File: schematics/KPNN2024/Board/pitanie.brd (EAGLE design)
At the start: 100 x 80 mm, 32 parts

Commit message: я смотрел рика и морти вместо работать
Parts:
- added R8: 1k, rcl:R0603
- added TMC: DRIVER_TMC2209, UNKNOWN-2024:DRIVER_TMC2209
- moved R7 138.1 mm to (68.6, 17.8)
- moved U$8 131.2 mm to (78.2, 21.0), turned to 225 degrees
- moved LSM 130.6 mm to (65.9, 48.3), turned to 90 degrees
- moved C8 129.4 mm to (64.8, 20.5)
- moved C10 127.2 mm to (69.9, 21.1)
- moved U$5 126.0 mm to (77.4, 26.4), turned to 270 degrees
- moved C4 120.6 mm to (72.6, 25.8), turned to 180 degrees
- moved LIS 118.3 mm to (39.9, 48.3), turned to 90 degrees
- moved C5 117.4 mm to (67.3, 31.5)
- moved C6 117.4 mm to (63.5, 31.5)
- moved C7 117.4 mm to (59.7, 31.5)
- moved U$2 115.8 mm to (72.9, 29.9), turned to 90 degrees
- moved C11 108.6 mm to (76.8, 30.7)
- moved U$1 106.2 mm to (54.9, 57.0), flipped to the bottom, turned to 180 degrees
- moved C12 103.3 mm to (42.9, 31.1)
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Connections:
- new net 5V: TMC.P$16
- new net A2: R8.2
- new net A3: R8.1, TMC.P$5
- net GND: now also TMC.P$15, TMC.P$8
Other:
- board size 100 x 80 mm -> 85.1 x 84.3 mm

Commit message: ааа платы платы полигоны разводка платы ааааа
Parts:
- C2, C6, C7: device rcl:C0603 -> rcl:C1206
- moved C4 75.7 mm to (47.3, 97.2)
- moved R3 74.0 mm to (44.1, 98.8)
- moved R2 73.8 mm to (40.8, 98.8)
- moved C5 73.2 mm to (44.1, 100.9), turned to 180 degrees
- moved U$2 70.9 mm to (43.1, 94.3), turned to 0 degrees
- moved U$3 70.0 mm to (52.4, 96.2), turned to 90 degrees
- moved R1 67.4 mm to (39.8, 87.6), turned to 270 degrees
- moved C7 58.7 mm to (49.5, 89.3)
- moved C6 57.2 mm to (49.5, 87.0)
- moved C2 48.6 mm to (43.8, 89.4), turned to 180 degrees
- moved C3 47.3 mm to (43.4, 86.9), turned to 180 degrees
- moved C1 46.3 mm to (39.9, 93.8)
- moved U$1 33.8 mm to (35.9, 85.0), flipped to the top, turned to 0 degrees
- moved R5 8.06 mm to (32.2, 36.2)
- moved C9 1.41 mm to (59.0, 23.0)
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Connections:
- removed net N$6: C5.1, C6.2, C7.2, R3.2, U$3.P$1
- net 3V3: now also C5.1, C6.2, C7.2, R3.2, U$3.P$1
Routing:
- net 3V3: track 0.00 -> 44.6 mm
- net GND-OUT: track 0.00 -> 42.7 mm, vias 0 -> 16
- net N$2: track 0.00 -> 14.6 mm, vias 0 -> 2
- net BUS+: track 0.00 -> 14.5 mm
- net N$5: track 0.00 -> 7.26 mm
- net N$1: track 0.00 -> 3.68 mm
- added copper zone on layer 1, net 3V3
- added copper zone on layer 1, net BUS+
- added copper zone on layer 1, net GND-OUT
- added copper zone on layer 1, net N$3
- added copper zone on layer 1, net N$4
- added copper zone on layer 1, net N$5

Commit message: авыпльдыф
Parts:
- C13, C14, C9: device rcl:C0603 -> rcl:C1206
- moved U$5 76.4 mm to (43.0, 94.7), turned to 0 degrees
- moved C8 76.3 mm to (40.0, 94.0), turned to 90 degrees
- moved C11 72.8 mm to (46.4, 96.8), turned to 180 degrees
- moved U$6 70.7 mm to (52.4, 97.2), turned to 90 degrees
- moved C10 70.6 mm to (44.1, 86.8), turned to 180 degrees
- moved C12 70.2 mm to (44.1, 101.3), turned to 180 degrees
- moved C9 68.5 mm to (44.4, 89.9), turned to 180 degrees
- moved R5 63.5 mm to (40.6, 99.2), turned to 180 degrees
- moved C13 63.5 mm to (50.0, 87.4), turned to 0 degrees
- moved C14 63.0 mm to (50.0, 89.9), turned to 0 degrees
- moved R6 62.9 mm to (44.2, 99.2), turned to 0 degrees
- moved C2 45.2 mm to (62.8, 48.4)
- moved C3 45.2 mm to (62.4, 45.9)
- moved C5 45.2 mm to (63.1, 59.9)
- moved U$1 45.2 mm to (54.9, 44.0)
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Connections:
- removed net N$12: C12.1, C13.2, C14.2, R6.2, U$6.P$1
- net 3V3: now also C12.1, C13.2, C14.2, R6.2, U$6.P$1
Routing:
- net 3V3: track 44.6 -> 88.4 mm
- net GND-OUT: track 42.7 -> 85.4 mm, vias 16 -> 32
- net BUS+: track 14.5 -> 29.9 mm
- net N$8: track 0.00 -> 14.2 mm, vias 0 -> 2
- net N$11: track 0.00 -> 7.51 mm
- net N$7: track 0.00 -> 3.93 mm
- added copper zone on layer 1, net N$10
- added copper zone on layer 1, net N$11
- added copper zone on layer 1, net N$9

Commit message: amogus
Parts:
- removed R8: 1k, rcl:R0603
- added U$10: PBS_SMD_X13, UNKNOWN-2024:PBD_SMD_X13
- added U$11: LIS3MDL, UNKNOWN-2024:LIS3MDL
- added U$9: PBS_SMD_X9, UNKNOWN-2024:PBS_SMD_X9
- moved U$1 55.7 mm to (36.7, 96.6), turned to 270 degrees
- moved R1 50.1 mm to (39.3, 92.7), turned to 180 degrees
- moved C3 49.3 mm to (38.6, 89.1), turned to 90 degrees
- moved C6 47.5 mm to (38.7, 83.0), turned to 270 degrees
- moved C2 45.8 mm to (41.1, 88.7), turned to 90 degrees
- moved C7 44.3 mm to (41.0, 83.0), turned to 270 degrees
- moved C1 42.0 mm to (45.5, 92.6), turned to 0 degrees
- moved U$2 39.5 mm to (46.0, 89.4), turned to 270 degrees
- moved U$4 38.1 mm to (72.3, 74.8), turned to 90 degrees
- moved R2 35.2 mm to (50.5, 91.7), turned to 90 degrees
- moved U$3 34.2 mm to (47.9, 80.1), turned to 0 degrees
- moved C4 33.8 mm to (48.9, 85.2), turned to 90 degrees
- moved R3 33.1 mm to (50.5, 88.4), turned to 270 degrees
- moved R4 31.0 mm to (69.5, 79.1), turned to 0 degrees
- moved C5 30.4 mm to (52.6, 88.4), turned to 90 degrees
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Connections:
- net A0 renamed FOTO
- net B10 renamed OE_SR
- removed net A2: R8.2
- removed net A3: R8.1, TMC.P$5
- removed net A5: LIS.P$4, LSM.P$4
- removed net A7: LIS.P$3, LSM.P$3, U$7.14
- removed net B2: U$7.11
- removed net B4: LIS.P$1, LSM.P$1
- new net DIR_DRIVER: TMC.P$1
- new net LATCH_SR: U$7.12
- new net MISO_SR: LSM.P$1, U$11.SDO
- new net MOSI_SR: LSM.P$3, U$11.SDA, U$7.14
- new net SCK_SR: LSM.P$4, U$11.SCL, U$7.11
- new net STEP_DRIVER: TMC.P$2
- net 3V3: now also U$11.UCC, U$7.16; no longer LIS.P$6
- net GND: now also U$11.GND, U$7.8; no longer LIS.P$5
- net Q1: now also U$11.CS; no longer LIS.P$2
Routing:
- net GND-OUT: track 85.4 -> 147.1 mm
- net N$3: track 0.00 -> 3.01 mm
- net BUS+: track 29.9 -> 32.7 mm
- net N$9: track 0.00 -> 1.82 mm
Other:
- board size 85.1 x 84.3 mm -> 68.9 x 68.9 mm

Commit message: отртамгор
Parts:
- removed LIS: LIS3MDL-GY, CanCubeSat:LIS3MDL-GY
- moved U$11 53.7 mm to (59.0, 50.0), turned to 90 degrees
- moved U$1 53.3 mm to (47.3, 44.4), turned to 90 degrees
- moved R2 45.7 mm to (33.5, 49.3), turned to 270 degrees
- moved C1 44.8 mm to (38.5, 48.4), turned to 180 degrees
- moved R1 44.7 mm to (44.7, 48.3), turned to 0 degrees
- moved C5 41.6 mm to (31.4, 52.6), turned to 270 degrees
- moved R3 39.6 mm to (33.5, 52.6), turned to 90 degrees
- moved U$2 38.6 mm to (38.0, 51.6), turned to 90 degrees
- moved C3 37.8 mm to (45.4, 51.9), turned to 270 degrees
- moved C2 36.4 mm to (42.9, 52.3), turned to 270 degrees
- moved C4 32.5 mm to (35.1, 55.8), turned to 270 degrees
- moved U$6 27.2 mm to (54.5, 65.0), turned to 270 degrees
- moved C6 25.9 mm to (45.3, 58.0), turned to 90 degrees
- moved C7 25.2 mm to (43.0, 58.0), turned to 90 degrees
- moved LSM 25.1 mm to (60.9, 30.7), turned to 270 degrees
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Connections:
- new net CE_RADIO: U$9.1
- new net CS_RADIO: U$9.2
- new net IRQ_RADIO: U$9.3
- new net MISO_RADIO: U$9.5
- new net MOSI_RADIO: U$9.4
- new net RX1_BLF: U$10.4
- new net RX2_GPS: U$9.8
- new net SCK_RADIO: U$9.6
- new net SW_AMP: U$9.9
- new net TX1_BLF: U$10.3
- new net TX2_GPS: U$9.7
- net 3V3: now also U$10.13
- net 5V: now also U$10.11
- net DIR_DRIVER: now also U$10.1
- net FOTO: now also U$10.10
- net GND: now also U$10.12
- net LATCH_SR: now also U$10.5
- net MISO_SR: now also U$10.8
- net MOSI_SR: now also U$10.9
- net OE_SR: now also U$10.6
- net SCK_SR: now also U$10.7
- net STEP_DRIVER: now also U$10.2
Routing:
- net GND: track 0.00 -> 124.7 mm, vias 0 -> 2
- net 3V3: track 88.3 -> 172.1 mm, vias 0 -> 4
- net MOSI_SR: track 0.00 -> 49.3 mm, vias 0 -> 2
- net BUS+: track 32.7 -> 81.7 mm, vias 0 -> 3
- net 5V: track 0.00 -> 43.6 mm, vias 0 -> 2
- net SCK_SR: track 0.00 -> 42.9 mm, vias 0 -> 1
- net OE_SR: track 0.00 -> 42.0 mm
- net FOTO: track 0.00 -> 35.1 mm
- net STEP_DRIVER: track 0.00 -> 33.4 mm
- net MISO_SR: track 0.00 -> 30.8 mm, vias 0 -> 3
- net LATCH_SR: track 0.00 -> 29.1 mm
- net Q1: track 0.00 -> 28.1 mm
- net DIR_DRIVER: track 0.00 -> 27.6 mm
- net GND-OUT: track 147.1 -> 167.5 mm
- net Q4: track 0.00 -> 16.6 mm, vias 0 -> 1

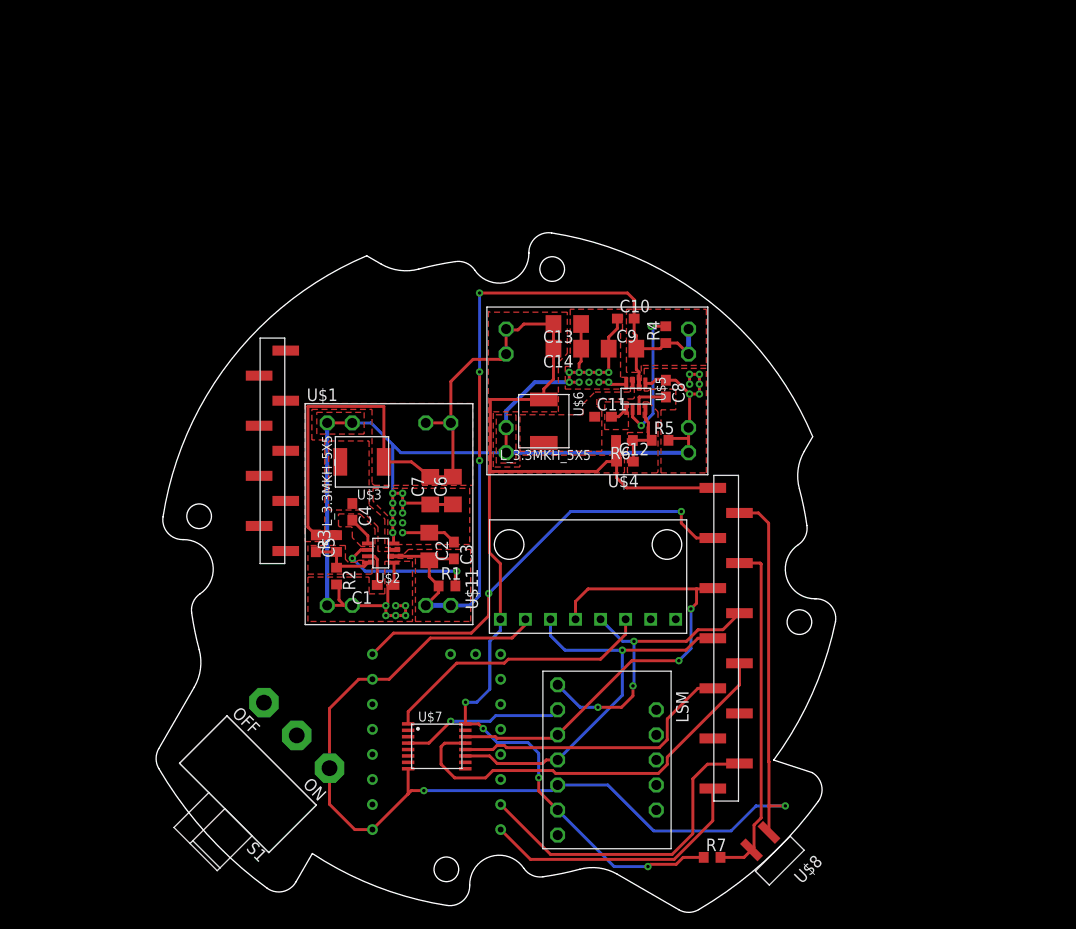
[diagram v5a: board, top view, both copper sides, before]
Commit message: Добавлены разъемы на плату питания
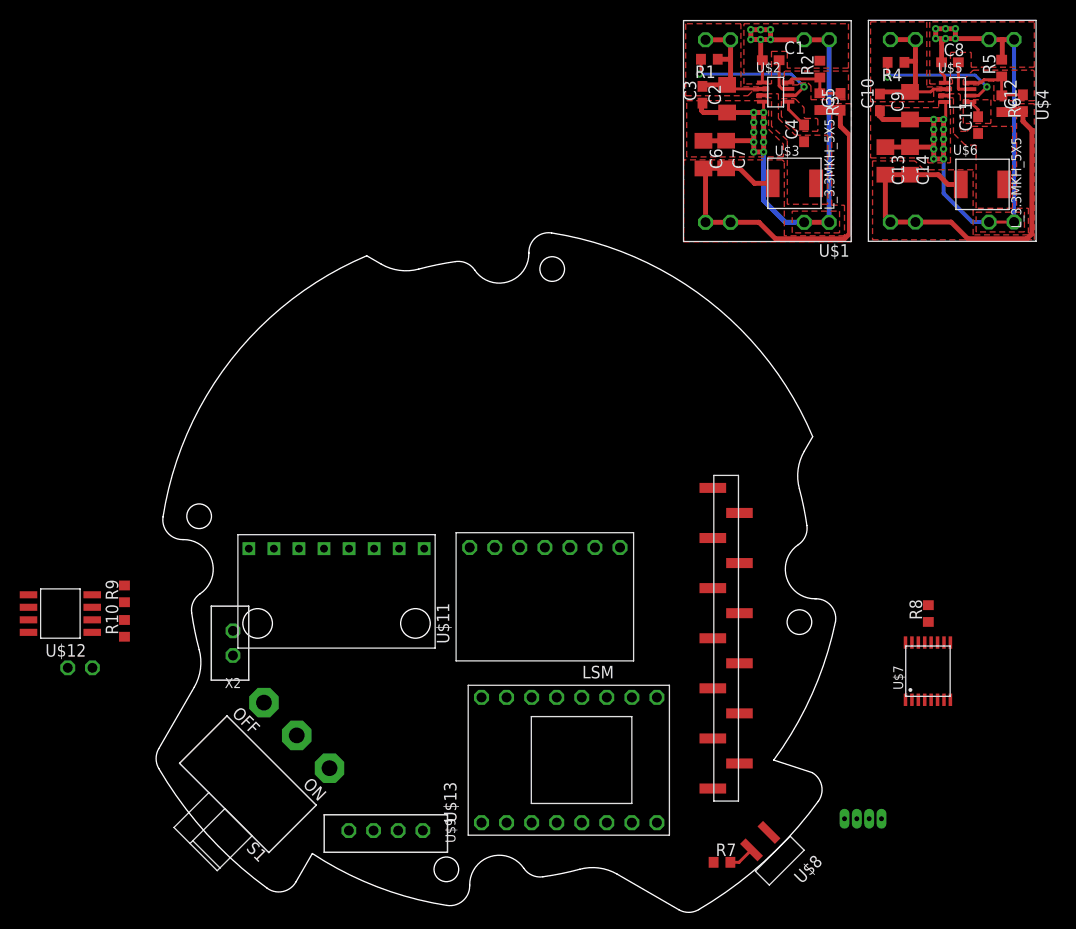
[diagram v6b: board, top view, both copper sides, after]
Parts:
- removed TMC: DRIVER_TMC2209, UNKNOWN-2024:DRIVER_TMC2209
- added R10, R8: 10k, rcl:R0603
- added R9: 100R, rcl:R0603
- added U$12: IRF7905PBF, UNKNOWN-2024:SO8
- added U$13: TMC2209_WITHOUT, UNKNOWN-2024:TMC2209_WITHOUT
- added U$14: MOLEX-4-1.25, UNKNOWN-2024:53047-04
- added X1, X2: JST-2-2.5, UNKNOWN-2024:JST-2-2.5
- LSM: value LSM6DS3-GY -> LSM6DS3_WITHOUT; device UNKNOWN-2024:LSM6DS3-GY -> UNKNOWN-2024:LSM6DS3_WITHOUT
- U$9: value PBS_SMD_X9 -> JST-4-2.5; device UNKNOWN-2024:PBS_SMD_X9 -> UNKNOWN-2024:JST-4-2.5
- moved R2 71.0 mm to (82.5, 100.7), turned to 90 degrees
- moved C5 69.5 mm to (84.6, 97.4), turned to 90 degrees
- moved R3 66.4 mm to (82.5, 97.4), turned to 270 degrees
- moved C1 66.0 mm to (77.5, 101.6), turned to 0 degrees
- moved U$1 64.9 mm to (68.7, 105.6), turned to 270 degrees
- moved U$2 61.5 mm to (78.0, 98.4), turned to 270 degrees
- moved C4 59.8 mm to (80.9, 94.2), turned to 90 degrees
- moved R1 59.7 mm to (71.3, 101.7), turned to 180 degrees
- moved C2 54.5 mm to (73.1, 97.7), turned to 90 degrees
- moved C12 54.3 mm to (103.1, 97.2), turned to 90 degrees
- moved C3 52.6 mm to (70.6, 98.1), turned to 90 degrees
- moved U$3 52.1 mm to (79.9, 89.1), turned to 0 degrees
- moved R6 51.3 mm to (101.0, 97.2), turned to 270 degrees
- moved R5 51.2 mm to (100.9, 100.8), turned to 90 degrees
- moved U$6 50.5 mm to (99.0, 89.0), turned to 0 degrees
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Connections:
- removed net 8V: S1.3
- removed net CE_RADIO: U$9.1
- removed net CS_RADIO: U$9.2
- removed net GND-OUT: C1.1, C10.1, C13.1, C14.1, C2.1, C3.1, C6.1, C7.1, C8.1, C9.1, R2.2, R5.2, U$1.P$3, U$1.P$4, U$1.P$5, U$1.P$6, U$2.P$1, U$2.P$4, U$4.P$3, U$4.P$4, U$4.P$5, U$4.P$6, U$5.P$1, U$5.P$4
- removed net IRQ_RADIO: U$9.3
- removed net MISO_RADIO: U$9.5
- removed net MOSI_RADIO: U$9.4
- removed net RX1_BLF: U$10.4
- removed net RX2_GPS: U$9.8
- removed net SCK_RADIO: U$9.6
- removed net SW_AMP: U$9.9
- removed net TX1_BLF: U$10.3
- removed net TX2_GPS: U$9.7
- new net A1: U$13.P$13, U$9.1
- new net A2: U$13.P$14, U$9.3
- new net B1: U$13.P$12, U$9.2
- new net B2: U$13.P$11, U$9.4
- new net BUS+_OUT: S1.1, X2.2
- new net EN_DRIVER: U$13.P$8
- new net N$6: R10.2, R9.1, U$12.2
- new net PERE_G: U$12.1, X1.2
- new net Q2: R9.2
- new net RX1_BLE: U$10.4, U$14.3
- new net TX1_BLE: U$10.3, U$14.4
- new net VCC: U$14.1
- net 3V3: now also LSM.P$2, R8.2, U$13.P$10, U$7.10; no longer C12.1, C13.2, C14.2, LSM.P$6, R6.2, U$4.P$7, U$4.P$8, U$6.P$1
- net 5V: now also C12.1, C13.2, C14.2, R6.2, U$13.P$16, U$4.P$7, U$4.P$8, U$6.P$1; no longer TMC.P$16
- net BUS+: now also S1.2, X1.1
- net DIR_DRIVER: now also U$13.P$1; no longer TMC.P$1
- net GND: now also C1.1, C10.1, C13.1, C14.1, C2.1, C3.1, C6.1, C7.1, C8.1, C9.1, LSM.P$3, R10.1, R2.2, R5.2, U$1.P$3, U$1.P$4, U$1.P$5, U$1.P$6, U$12.7, U$12.8, U$13.P$15, U$13.P$9, U$14.2, U$2.P$1, U$2.P$4, U$4.P$3, U$4.P$4, U$4.P$5, U$4.P$6, U$5.P$1, U$5.P$4, X2.1; no longer LSM.P$5, S1.1, TMC.P$15, TMC.P$8
- net MISO_SR: now also LSM.P$7; no longer LSM.P$1
- net MOSI_SR: now also LSM.P$5; no longer LSM.P$3
- net OE_SR: now also R8.1
- net Q4: now also LSM.P$6; no longer LSM.P$2
- net STEP_DRIVER: now also U$13.P$2; no longer TMC.P$2
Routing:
- net GND-OUT: track 167.5 -> 0.00 mm, vias 32 -> 0
- net 3V3: track 172.1 -> 43.8 mm, vias 4 -> 0
- net BUS+: track 81.7 -> 30.9 mm, vias 3 -> 0
- net MOSI_SR: track 49.3 -> 0.00 mm, vias 2 -> 0
- net SCK_SR: track 42.9 -> 0.00 mm, vias 1 -> 0
- net OE_SR: track 42.0 -> 0.00 mm
- net STEP_DRIVER: track 33.4 -> 0.00 mm
- net FOTO: track 35.1 -> 2.67 mm
- net MISO_SR: track 30.8 -> 0.00 mm, vias 3 -> 0
- net LATCH_SR: track 29.1 -> 0.00 mm
- net Q1: track 28.1 -> 0.00 mm
- net DIR_DRIVER: track 27.6 -> 0.00 mm
- net GND: track 124.7 -> 142.6 mm, vias 2 -> 32
- net Q4: track 16.6 -> 0.00 mm, vias 1 -> 0
- net 5V: track 43.6 -> 43.3 mm, vias 2 -> 0
- added copper zone on layer 1, net GND
- removed copper zone on layer 1, net GND-OUT

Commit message: Разведена плата питания
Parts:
- moved U$7 53.7 mm to (40.3, 32.3)
- moved C10 46.3 mm to (52.1, 68.8)
- moved C12 46.3 mm to (66.6, 68.7)
- moved C13 46.3 mm to (52.6, 62.9)
- moved C14 46.3 mm to (55.1, 62.9)
- moved C8 46.3 mm to (59.2, 72.9)
- moved C9 46.3 mm to (55.1, 68.5)
- moved R4 46.3 mm to (53.7, 72.9)
- moved R5 46.3 mm to (64.4, 72.3)
- moved R6 46.3 mm to (64.5, 68.7)
- moved U$4 46.3 mm to (50.9, 77.1)
- moved U$6 46.3 mm to (62.5, 60.5)
- moved C11 46.3 mm to (62.0, 66.5)
- moved U$5 46.3 mm to (60.0, 69.8)
- moved C4 45.9 mm to (44.9, 65.7)
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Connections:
- removed net BUZZER: U$7.7
- removed net Q1: U$11.CS, U$7.1
- removed net Q2: R9.2
- removed net Q4: LSM.P$6, U$7.4
- removed net VCC: U$14.1
- new net CS_LIS: U$11.CS, U$7.2
- new net CS_LSM: LSM.P$6, U$7.6
- new net PERE: R9.2, U$7.1
- net 5V: now also U$14.1
- net EN_DRIVER: now also U$7.7
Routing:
- net GND: track 142.6 -> 339.7 mm, vias 32 -> 36
- net 3V3: track 43.8 -> 160.1 mm, vias 0 -> 4
- net 5V: track 43.3 -> 129.8 mm, vias 0 -> 2
- net BUS+: track 30.9 -> 98.8 mm
- net MOSI_SR: track 0.00 -> 57.1 mm, vias 0 -> 1
- net SCK_SR: track 0.00 -> 51.3 mm
- net OE_SR: track 0.00 -> 49.8 mm
- net MISO_SR: track 0.00 -> 43.9 mm
- net FOTO: track 2.67 -> 44.6 mm, vias 0 -> 2
- net LATCH_SR: track 0.00 -> 40.4 mm
- net B2: track 0.00 -> 35.7 mm, vias 0 -> 1
- net EN_DRIVER: track 0.00 -> 31.4 mm
- net PERE: track 0.00 -> 31.1 mm
- net B1: track 0.00 -> 29.6 mm
- net A2: track 0.00 -> 28.7 mm
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- added copper zone on layer 1, net 5V
- added copper zone on layer 16, net GND
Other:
- board size 68.9 x 68.9 mm -> 68.9 x 68.2 mm

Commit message: ждангнгорлек самолзшщапнготреап ияч пнгеапорвап тапоршл
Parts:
- C1, C11, C2, C4, C8, C9: value (none) -> 0,1u
- C10, C13, C14, C3, C6, C7: value (none) -> 22u
- C12, C5: value (none) -> 33p
- L_3.3, U$6: value L_3.3MKH_5X5 -> L_3.3MKH
- R1, R4: value (none) -> 100k
- R2, R5: value (none) -> 8k87
- R3, R6: value (none) -> 40k2
- flipped U$13 to the bottom
- renumbered U$3 to L_3.3
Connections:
- net DIR_DRIVER: now also U$10.2; no longer U$10.1
- net STEP_DRIVER: now also U$10.1; no longer U$10.2
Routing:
- net 5V: track 129.8 -> 108.6 mm
- net EN_DRIVER: track 31.4 -> 10.9 mm
- net DIR_DRIVER: track 17.1 -> 34.1 mm
- net B2: track 35.7 -> 27.0 mm, vias 1 -> 0
- net STEP_DRIVER: track 22.6 -> 27.9 mm
- net A2: track 28.7 -> 33.0 mm, vias 0 -> 1
- net 3V3: track 160.1 -> 163.4 mm
- net B1: track 29.6 -> 26.4 mm
- net A1: track 27.6 -> 27.4 mm, vias 1 -> 0
